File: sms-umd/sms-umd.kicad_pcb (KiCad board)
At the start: 2 copper layers, 5 parts, among them CON101 UMDv2-CONN, CON102 SMS-CONN, CON103 JTAG-2X5-HDR, U101 MCP23008T-E_SS

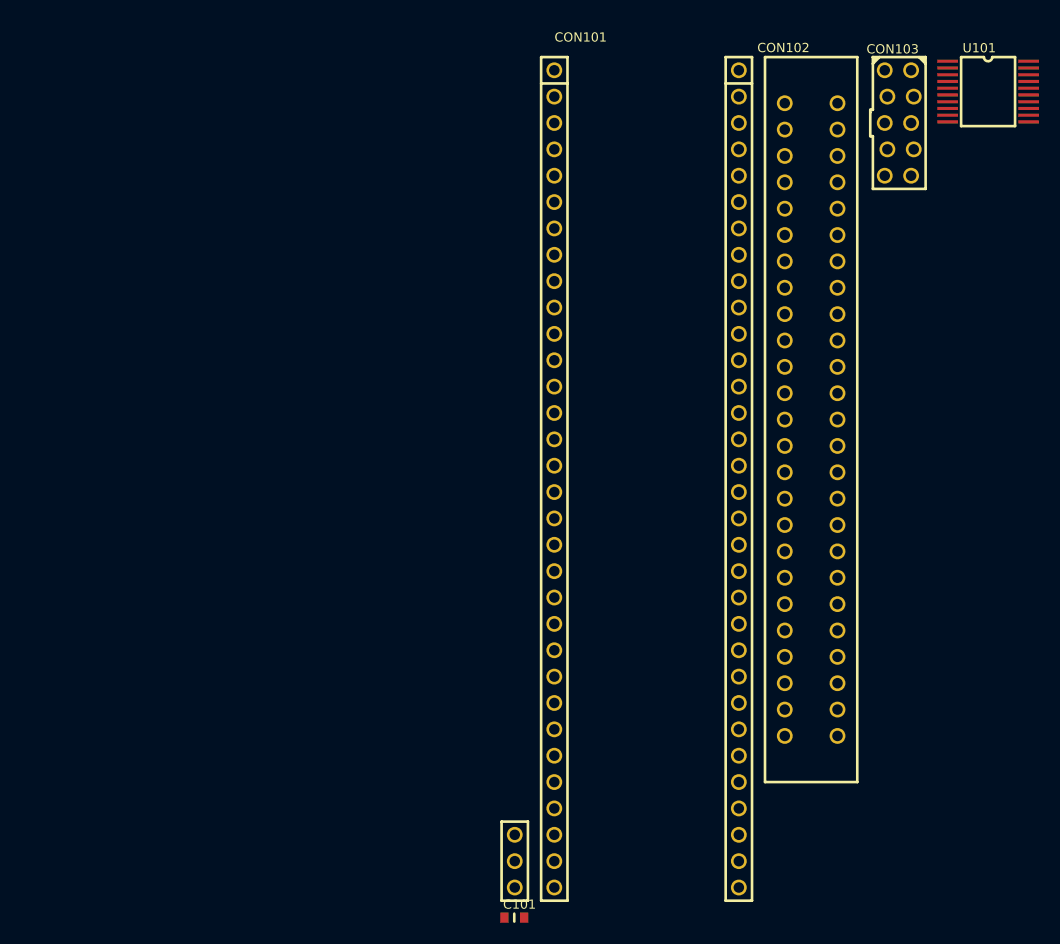
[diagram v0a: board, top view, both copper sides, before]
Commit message: started laying out and routing the PCB
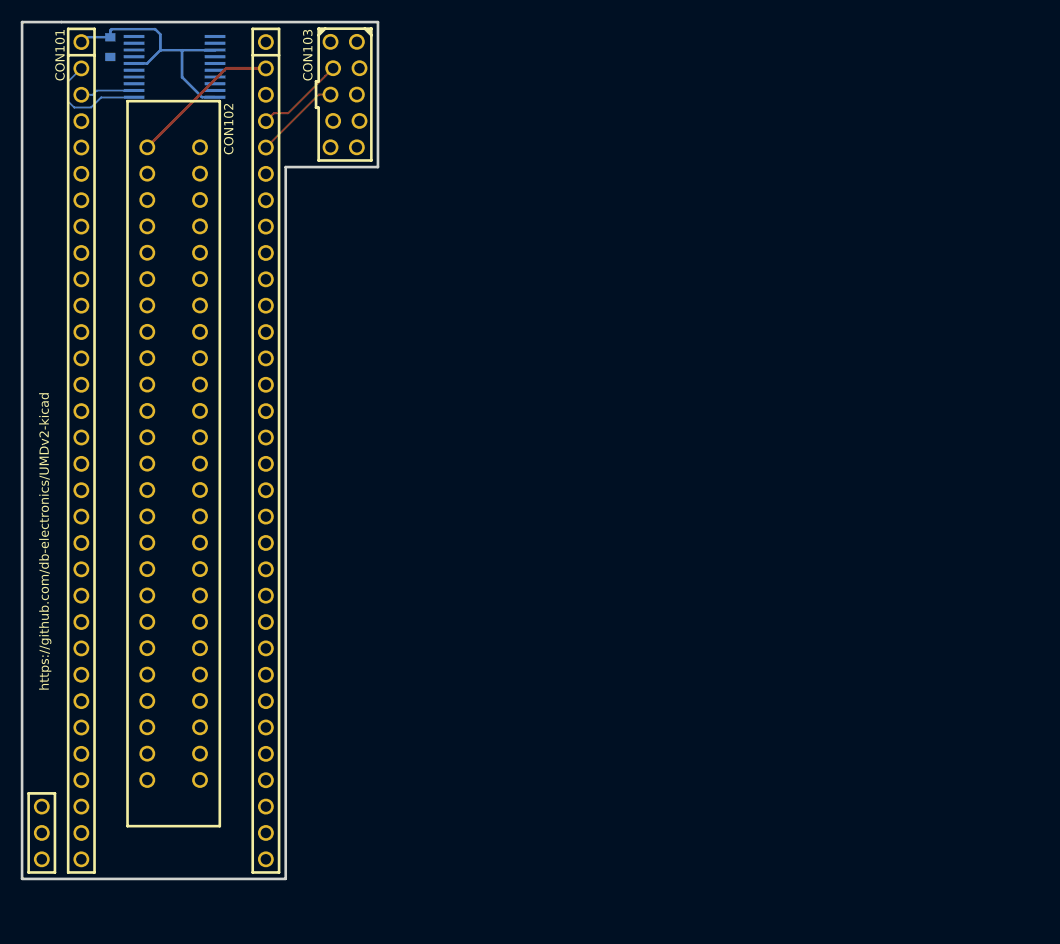
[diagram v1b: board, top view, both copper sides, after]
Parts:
- C101, U101: moved to B.Cu
- moved C101 92.5 mm to (138.8, 59.3), turned to 270 degrees
- moved U101 78.5 mm to (141.0, 64.1)
- moved CON102 61.6 mm to (142.3, 68.9)
- moved CON103 53.5 mm to (160.1, 58.8)
- moved CON101 45.6 mm to (136.0, 58.8)
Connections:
- net /~M1~ renamed Net-(CON102-Pad37)
- CON101 pad 64: Net-(CON101-Pad64) -> GND
- CON102 pad 1: Net-(CON102-Pad1) -> /5V_0
- CON102 pad 47: /CLK -> /TCK
- U101 pad 6: GND -> +3V3
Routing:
- net +3V3: track 0.00 -> 25.2 mm
- net /5V_0: track 0.00 -> 14.5 mm
- net /SCL: track 0.00 -> 10.7 mm
- net /TDO: track 0.00 -> 8.59 mm
- net /TMS: track 0.00 -> 8.34 mm
- net /SDA: track 0.00 -> 5.25 mm
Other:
- board outline added: 34.3 x 82.5 mm
- net class Default: clearance 0.2 -> 0.1778; trace_width 0.25 -> 0.1778; via_dia 0.8 -> 0.6096; via_drill 0.4 -> 0.3048
- net class power added: clearance 0.1778, trace_width 0.254, via_dia 0.6096, via_drill 0.3048
- rule trace_clearance: 0.2 -> 0.1778
- rule trace_min: 0.2 -> 0.1778
- rule via_min_size: 0.4 -> 0.3048
- board text added: "https://github.com/db-electronics/UMDv2-kicad"

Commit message: prelim routing completed
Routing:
- net /TCK: track 0.00 -> 104.9 mm
- net /~RST~: track 0.00 -> 71.4 mm
- net /~MREQ~: track 0.00 -> 51.9 mm
- net /A15: track 0.00 -> 50.8 mm, vias 0 -> 3
- net /A4: track 0.00 -> 48.4 mm
- net /A12: track 0.00 -> 47.8 mm, vias 0 -> 3
- net /A2: track 0.00 -> 42.0 mm
- net /TDI: track 0.00 -> 40.5 mm
- net /A1: track 0.00 -> 38.1 mm
- net /A0: track 0.00 -> 37.2 mm
- net /~CE~: track 0.00 -> 35.8 mm, vias 0 -> 1
- net /A3: track 0.00 -> 32.7 mm
- net /5V_1: track 0.00 -> 31.8 mm
- net /A7: track 0.00 -> 31.3 mm
- net /A6: track 0.00 -> 31.3 mm
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- added copper zone on B.Cu, net GND
- added copper zone on F.Cu, net GND
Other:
- outline, holes or cut-outs redrawn

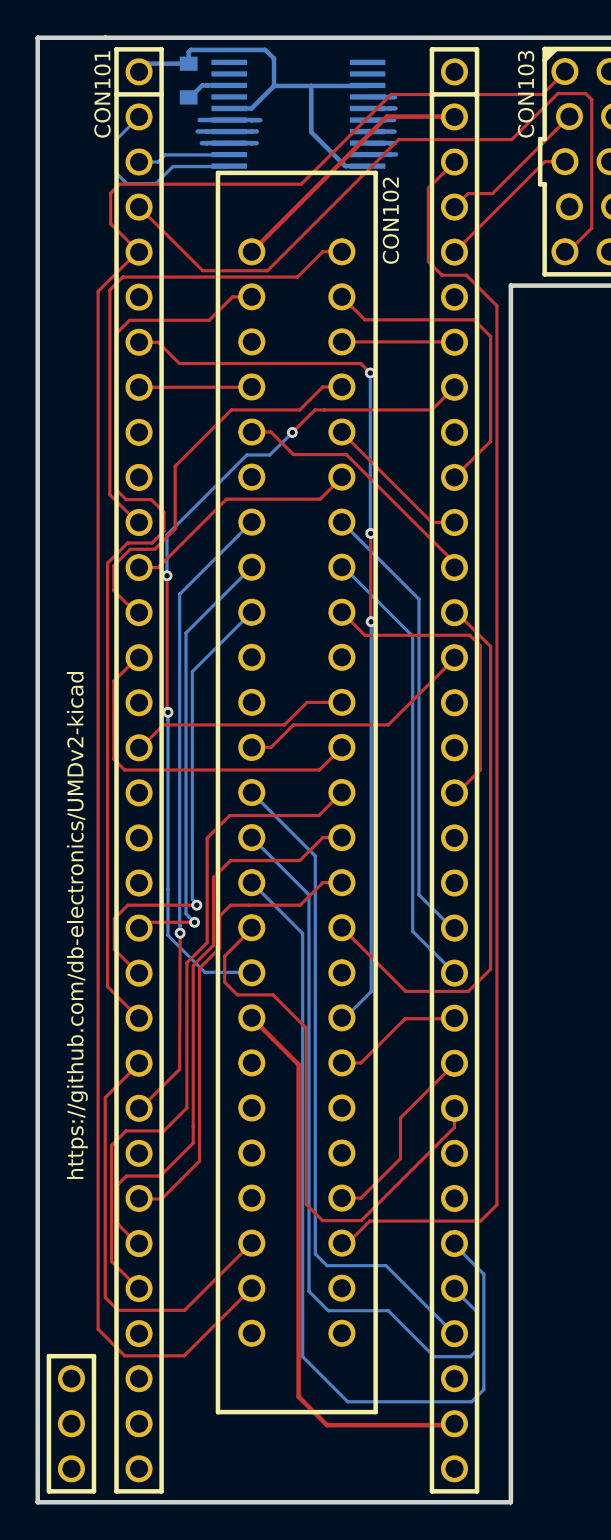
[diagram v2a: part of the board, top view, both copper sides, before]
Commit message: added OSHWA marking for v1.0 release
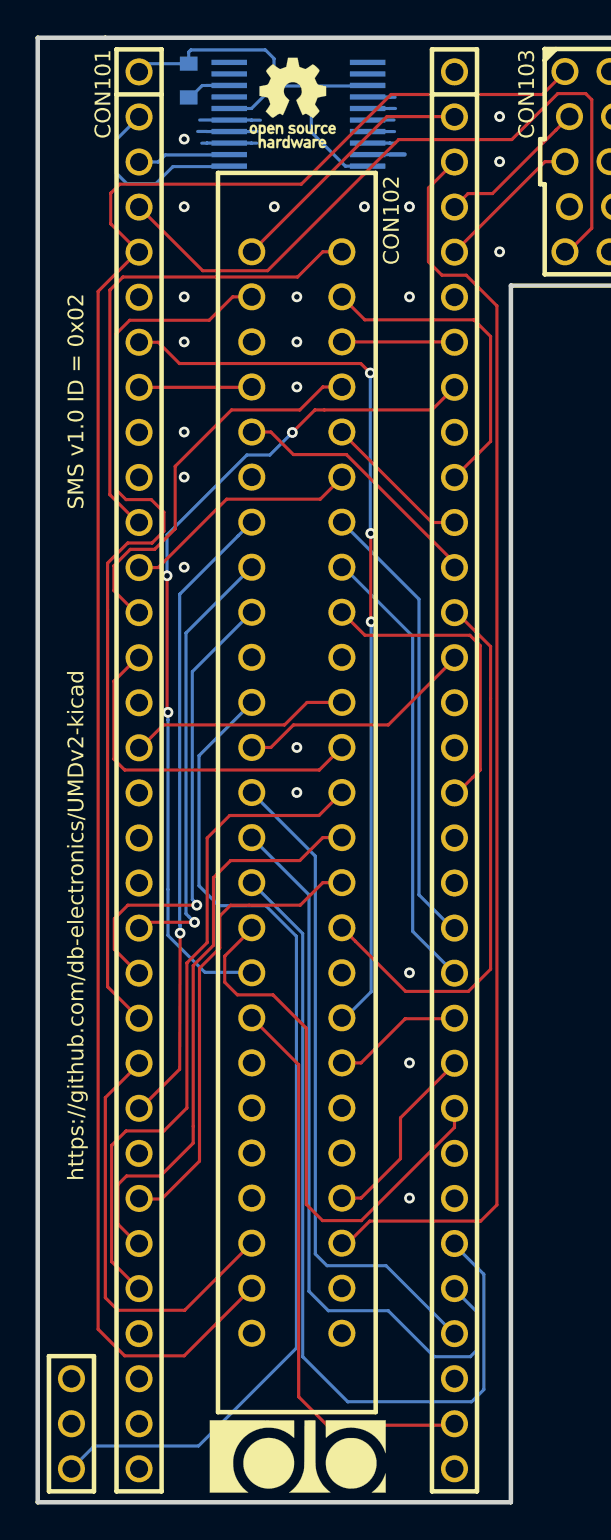
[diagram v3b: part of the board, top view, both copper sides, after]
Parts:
- added G***: LOGO, db-artwork:oshw-logo_5mm, F.Cu at (144.6, 60.5)
- added G***: LOGO, db-artwork:db-logo_10mm, F.Cu at (144.9, 136.8)
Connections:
- CON102 pad 21: GND -> /~CART~
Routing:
- net /~CART~: track 0.00 -> 56.8 mm
- net GND: track 21.6 -> 22.5 mm, vias 0 -> 22
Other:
- board text added: "SMS v1.0 ID = 0x02"
